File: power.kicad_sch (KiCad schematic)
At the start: 27 parts, among them IC1 SI2301CDS-T1-GE3, J1 Barrel_Jack_MountingPin, J2 Conn_02x04_Odd_Even, U1 TMA-1212D, U2 TPS54302

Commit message: TVS fix
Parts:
- added D13, D14: SMBJ15CA, Diode_SMD:D_SMB, symbol Device:D_TVS
- D1: value D_TVS -> SMBJ15CA
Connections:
- net GND: now also D13.2 (A2), D14.2 (A2)
- net at C2.1, L2.1, U1.6 (+Vout): now also D13.1 (A1), D14.1 (A1)
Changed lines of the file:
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@@
 	)
 	(junction
+		(at 87.63 147.32)
+		(diameter 0)
+		(color 0 0 0 0)
+	)
+	(junction
 		(at 80.01 133.35)
 		(diameter 0)
@@
 	)
 	(junction
+		(at 82.55 128.27)
+		(diameter 0)
+		(color 0 0 0 0)
+	)
+	(junction
 		(at 91.44 49.53)
 		(diameter 0)
@@
 	)
 	(junction
+		(at 93.98 128.27)
+		(diameter 0)
+		(color 0 0 0 0)
+	)
+	(junction
 		(at 161.29 88.9)
 		(diameter 0)
@@
 	(wire
 		(pts
+			(xy 80.01 147.32) (xy 80.01 165.1)
+		)
+		(stroke
+			(width 0)
+			(type default)
+		)
+	)
+	(wire
+		(pts
 			(xy 231.14 128.27) (xy 233.68 128.27)
 		)
@@
 	(wire
 		(pts
-			(xy 71.12 128.27) (xy 88.9 128.27)
+			(xy 71.12 128.27) (xy 82.55 128.27)
 		)
 		(stroke
@@
 	(wire
 		(pts
+			(xy 87.63 152.4) (xy 87.63 147.32)
+		)
+		(stroke
+			(width 0)
+			(type default)
+		)
+	)
+	(wire
+		(pts
 			(xy 80.01 133.35) (xy 95.25 133.35)
 		)
@@
 	(wire
 		(pts
+			(xy 93.98 152.4) (xy 87.63 152.4)
+		)
+		(stroke
+			(width 0)
+			(type default)
+		)
+	)
+	(wire
+		(pts
 			(xy 156.21 118.11) (xy 132.08 118.11)
 		)
@@
 	(wire
 		(pts
-			(xy 80.01 144.78) (xy 80.01 147.32)
-		)
-		(stroke
-			(width 0)
-			(type default)
-		)
-	)
-	(wire
-		(pts
 			(xy 50.8 133.35) (xy 49.53 133.35)
 		)
@@
 	(wire
 		(pts
-			(xy 88.9 147.32) (xy 80.01 147.32)
+			(xy 88.9 147.32) (xy 87.63 147.32)
 		)
 		(stroke
@@
 	(wire
 		(pts
+			(xy 82.55 128.27) (xy 88.9 128.27)
+		)
+		(stroke
+			(width 0)
+			(type default)
+		)
+	)
+	(wire
+		(pts
 			(xy 71.12 133.35) (xy 80.01 133.35)
 		)
@@
 	(wire
 		(pts
+			(xy 82.55 128.27) (xy 82.55 157.48)
+		)
+		(stroke
+			(width 0)
+			(type default)
+		)
+	)
+	(wire
+		(pts
 			(xy 140.97 66.04) (xy 140.97 62.23)
 		)
@@
 	(wire
 		(pts
+			(xy 82.55 165.1) (xy 80.01 165.1)
+		)
+		(stroke
+			(width 0)
+			(type default)
+		)
+	)
+	(wire
+		(pts
 			(xy 205.74 134.62) (xy 214.63 134.62)
 		)
@@
 	(wire
 		(pts
+			(xy 93.98 128.27) (xy 100.33 128.27)
+		)
+		(stroke
+			(width 0)
+			(type default)
+		)
+	)
+	(wire
+		(pts
 			(xy 80.01 49.53) (xy 74.93 49.53)
 		)
@@
 	(wire
 		(pts
-			(xy 88.9 128.27) (xy 100.33 128.27)
+			(xy 88.9 128.27) (xy 93.98 128.27)
 		)
 		(stroke
@@
 	(wire
 		(pts
+			(xy 93.98 144.78) (xy 93.98 128.27)
+		)
+		(stroke
+			(width 0)
+			(type default)
+		)
+	)
+	(wire
+		(pts
+			(xy 87.63 147.32) (xy 80.01 147.32)
+		)
+		(stroke
+			(width 0)
+			(type default)
+		)
+	)
+	(wire
+		(pts
 			(xy 184.15 129.54) (xy 184.15 133.35)
 		)
@@
 		)
 	)
+	(wire
+		(pts
+			(xy 80.01 144.78) (xy 80.01 147.32)
+		)
+		(stroke
+			(width 0)
+			(type default)
+		)
+	)
 	(label "+12V_IN"
 		(at 39.37 46.99 0)
@@
 	)
 	(symbol
+		(lib_id "Device:D_TVS")
+		(at 82.55 161.29 270)
+		(unit 1)
+		(exclude_from_sim no)
+		(in_bom yes)
+		(on_board yes)
+		(dnp no)
+		(property "Reference" "D14"
+			(at 84.836 155.956 90)
+			(effects
+				(font
+					(size 1.27 1.27)
+				)
+			)
+		)
+		(property "Value" "SMBJ15CA"
+			(at 87.63 157.734 90)
+			(effects
+				(font
+					(size 1.27 1.27)
+				)
+			)
+		)
+		(property "Footprint" "Diode_SMD:D_SMB"
+			(at 82.55 161.29 0)
+			(effects
+				(font
+					(size 1.27 1.27)
+				)
+				(hide yes)
+			)
+		)
+		(property "Datasheet" "~"
+			(at 82.55 161.29 0)
+			(effects
+				(font
+					(size 1.27 1.27)
+				)
+				(hide yes)
+			)
+		)
+		(property "Description" "Bidirectional transient-voltage-suppression diode"
+			(at 82.55 161.29 0)
+			(effects
+				(font
+					(size 1.27 1.27)
+				)
+				(hide yes)
+			)
+		)
+		(pin "1"
+		)
+		(pin "2"
+		)
+		(instances
+			(project "daisy-studio"
+				(path "/55cca6a8-30da-4c13-b2f2-a01401e2b54c/a1b2c3d4-1111-4000-8000-000000000001"
+					(reference "D14")
+					(unit 1)
+				)
+			)
+		)
+	)
+	(symbol
 		(lib_id "Device:L")
 		(at 99.06 133.35 90)
@@
 			)
 		)
-		(property "Value" "D_TVS"
+		(property "Value" "SMBJ15CA"
 			(at 85.09 53.594 90)
 			(effects
@@
 					(size 1.27 1.27)
 				)
+				(hide yes)
 			)
 		)
@@
 					(size 1.27 1.27)
 				)
+				(hide yes)
 			)
 		)
@@
 					(unit 1)
 				)
+			)
+		)
+	)
+	(symbol
+		(lib_id "Device:D_TVS")
+		(at 93.98 148.59 270)
+		(unit 1)
+		(exclude_from_sim no)
+		(in_bom yes)
+		(on_board yes)
+		(dnp no)
+		(property "Reference" "D13"
+			(at 96.266 143.256 90)
+			(effects
+				(font
+					(size 1.27 1.27)
+				)
+			)
+		)
+		(property "Value" "SMBJ15CA"
+			(at 99.06 145.034 90)
+			(effects
+				(font
+					(size 1.27 1.27)
+				)
+			)
+		)
+		(property "Footprint" "Diode_SMD:D_SMB"
+			(at 93.98 148.59 0)
+			(effects
+				(font
+					(size 1.27 1.27)
+				)
+				(hide yes)
+			)
+		)
+		(property "Datasheet" "~"
+			(at 93.98 148.59 0)
+			(effects
+				(font
+					(size 1.27 1.27)
+				)
+				(hide yes)
+			)
+		)
+		(property "Description" "Bidirectional transient-voltage-suppression diode"
+			(at 93.98 148.59 0)
+			(effects
+				(font
+					(size 1.27 1.27)
+				)
+				(hide yes)
+			)
+		)
+		(pin "1"
+		)
+		(pin "2"
+		)
+		(instances
+			(project "daisy-studio"
+				(path "/55cca6a8-30da-4c13-b2f2-a01401e2b54c/a1b2c3d4-1111-4000-8000-000000000001"
+					(reference "D13")
+					(unit 1)
+				)

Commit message: working on output
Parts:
- removed J2: Conn_02x04_Odd_Even, Connector_PinHeader_2.54mm:PinHeader_2x04_P2.54mm_Vertical, symbol Connector_Generic:Conn_02x04_Odd_Even
- added J14: Conn_02x04_Odd_Even, Connector_PinHeader_2.54mm:PinHeader_2x04_P2.54mm_Vertical, symbol Connector:Conn_01x04_Pin
- added J2: Conn_02x04_Odd_Even, Connector_PinHeader_2.54mm:PinHeader_2x04_P2.54mm_Vertical, symbol Connector:Conn_01x05_Pin
- renumbered D14 to D2, D13 to D3
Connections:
- net +12VA: now also D2.2 (A2), J2.1 (Pin_1)
- net +3V3A: now also J2.3 (Pin_3)
- net +3V3D: now also J14.1 (Pin_1)
- net +5V: now also J14.4 (Pin_4)
- net -12VA: now also D3.1 (A1), J2.5 (Pin_5)
- net GND: now also D2.1 (A1), J14.2 (Pin_2), J14.3 (Pin_3), J2.2 (Pin_2), J2.4 (Pin_4); no longer D2.2 (A2)
- net at C2.1, L2.1, U1.6 (+Vout): no longer D2.1 (A1), D3.1 (A1)
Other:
- moved on the sheet: D2, D3

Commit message: fix seed schematic
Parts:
- renumbered J14 to J3
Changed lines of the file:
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@@
 		(on_board yes)
 		(dnp no)
-		(property "Reference" "#PWR013"
+		(property "Reference" "#PWR014"
 			(at 190.5 132.08 0)
 			(effects
@@
 			(project "daisy-studio"
 				(path "/55cca6a8-30da-4c13-b2f2-a01401e2b54c/a1b2c3d4-1111-4000-8000-000000000001"
-					(reference "#PWR013")
+					(reference "#PWR014")
 					(unit 1)
 				)
@@
 		(on_board yes)
 		(dnp no)
-		(property "Reference" "#PWR012"
+		(property "Reference" "#PWR013"
 			(at 168.91 148.59 0)
 			(effects
@@
 			(project "triptech"
 				(path "/55cca6a8-30da-4c13-b2f2-a01401e2b54c/a1b2c3d4-1111-4000-8000-000000000001"
-					(reference "#PWR012")
+					(reference "#PWR013")
 					(unit 1)
 				)
@@
 		(dnp no)
 		(fields_autoplaced yes)
-		(property "Reference" "#PWR014"
+		(property "Reference" "#PWR015"
 			(at 205.74 148.59 0)
 			(effects
@@
 			(project "daisy-studio"
 				(path "/55cca6a8-30da-4c13-b2f2-a01401e2b54c/a1b2c3d4-1111-4000-8000-000000000001"
-					(reference "#PWR014")
+					(reference "#PWR015")
 					(unit 1)
 				)
@@
 		(on_board yes)
 		(dnp no)
-		(property "Reference" "J14"
+		(property "Reference" "J3"
 			(at 160.274 132.588 90)
 			(effects
@@
 			(project "daisy-studio"
 				(path "/55cca6a8-30da-4c13-b2f2-a01401e2b54c/a1b2c3d4-1111-4000-8000-000000000001"
-					(reference "J14")
+					(reference "J3")
 					(unit 1)
 				)
@@
 		(on_board yes)
 		(dnp no)
-		(property "Reference" "#PWR016"
+		(property "Reference" "#PWR017"
 			(at 231.14 149.86 0)
 			(effects
@@
 			(project "daisy-studio"
 				(path "/55cca6a8-30da-4c13-b2f2-a01401e2b54c/a1b2c3d4-1111-4000-8000-000000000001"
-					(reference "#PWR016")
+					(reference "#PWR017")
 					(unit 1)
 				)
@@
 		(dnp no)
 		(fields_autoplaced yes)
-		(property "Reference" "#PWR015"
+		(property "Reference" "#PWR016"
 			(at 210.82 96.52 0)
 			(effects
@@
 			(project "triptech"
 				(path "/55cca6a8-30da-4c13-b2f2-a01401e2b54c/a1b2c3d4-1111-4000-8000-000000000001"
-					(reference "#PWR015")
+					(reference "#PWR016")
 					(unit 1)
 				)
@@
 		(dnp no)
 		(fields_autoplaced yes)
-		(property "Reference" "#PWR089"
+		(property "Reference" "#PWR011"
 			(at 154.94 157.48 0)
 			(effects
@@
 			(project "daisy-studio"
 				(path "/55cca6a8-30da-4c13-b2f2-a01401e2b54c/a1b2c3d4-1111-4000-8000-000000000001"
-					(reference "#PWR089")
+					(reference "#PWR011")
 					(unit 1)
 				)
@@
 		(dnp no)
 		(fields_autoplaced yes)
-		(property "Reference" "#PWR017"
+		(property "Reference" "#PWR018"
 			(at 233.68 52.07 0)
 			(effects
@@
 			(project ""
 				(path "/55cca6a8-30da-4c13-b2f2-a01401e2b54c/a1b2c3d4-1111-4000-8000-000000000001"
-					(reference "#PWR017")
+					(reference "#PWR018")
 					(unit 1)
 				)
@@
 		(on_board yes)
 		(dnp no)
-		(property "Reference" "#PWR011"
+		(property "Reference" "#PWR012"
 			(at 157.48 146.05 0)
 			(effects
@@
 			(project "daisy-studio"
 				(path "/55cca6a8-30da-4c13-b2f2-a01401e2b54c/a1b2c3d4-1111-4000-8000-000000000001"
-					(reference "#PWR011")
+					(reference "#PWR012")
 					(unit 1)
 				)

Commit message: fix up power values
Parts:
- C1, C2: value C -> 10u
- C3, C5: value C -> 100n
- C4: value C_Polarized -> 100u
- C6, C7: value C -> 22u
- C8: value C -> 75p
- L1, L2: value L -> BLM18PG121SN1
- L3: value L -> 10uH
- R1: value R -> 10k
- R2: value R -> 100k
- R3: value R -> 13.7k 1%
- R4: value R -> 49k9 1%
- R5: value R -> 100k 1%
- R6: value R -> 13k3 1%
- renumbered IC1 to Q?
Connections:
- no-connect marks 1 -> 0
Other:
- moved on the sheet: J1

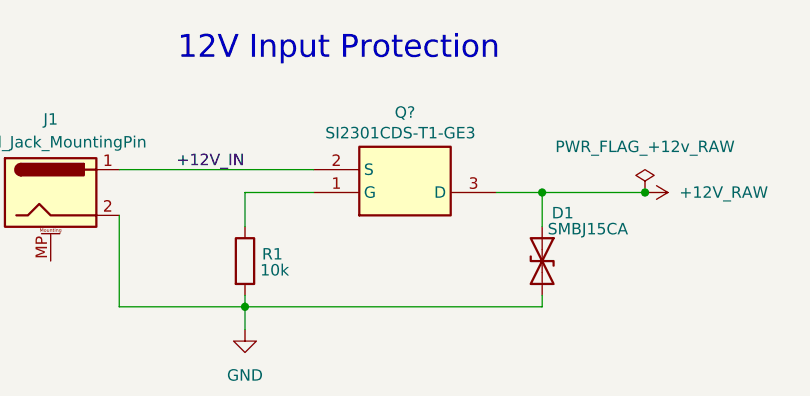
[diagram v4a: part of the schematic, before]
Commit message: reannotate, fix cap footprints
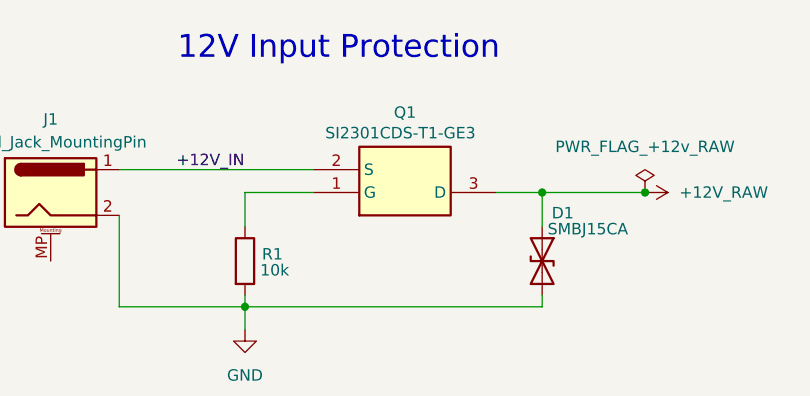
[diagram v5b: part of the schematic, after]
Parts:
- C6, C7: footprint Capacitor_SMD:C_0805_2012Metric -> Capacitor_SMD:C_1206_3216Metric
- gave numbers to parts that had none: 1
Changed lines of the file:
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@@
 			)
 		)
-		(property "Footprint" "Capacitor_SMD:C_0805_2012Metric"
+		(property "Footprint" "Capacitor_SMD:C_1206_3216Metric"
 			(at 211.7852 62.23 0)
 			(effects
@@
 		(on_board yes)
 		(dnp no)
-		(property "Reference" "Q?"
+		(property "Reference" "Q1"
 			(at 64.77 40.64 0)
 			(effects
@@
 			(project "triptech"
 				(path "/55cca6a8-30da-4c13-b2f2-a01401e2b54c/a1b2c3d4-1111-4000-8000-000000000001"
-					(reference "Q?")
+					(reference "Q1")
 					(unit 1)
 				)
@@
 			)
 		)
-		(property "Footprint" "Capacitor_SMD:C_0805_2012Metric"
+		(property "Footprint" "Capacitor_SMD:C_1206_3216Metric"
 			(at 202.8952 62.23 0)
 			(effects

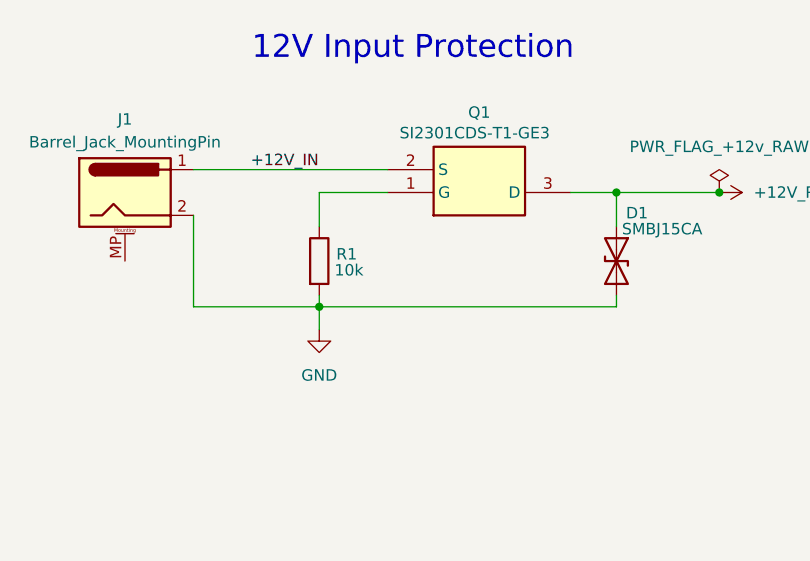
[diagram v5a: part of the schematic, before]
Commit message: add power switch
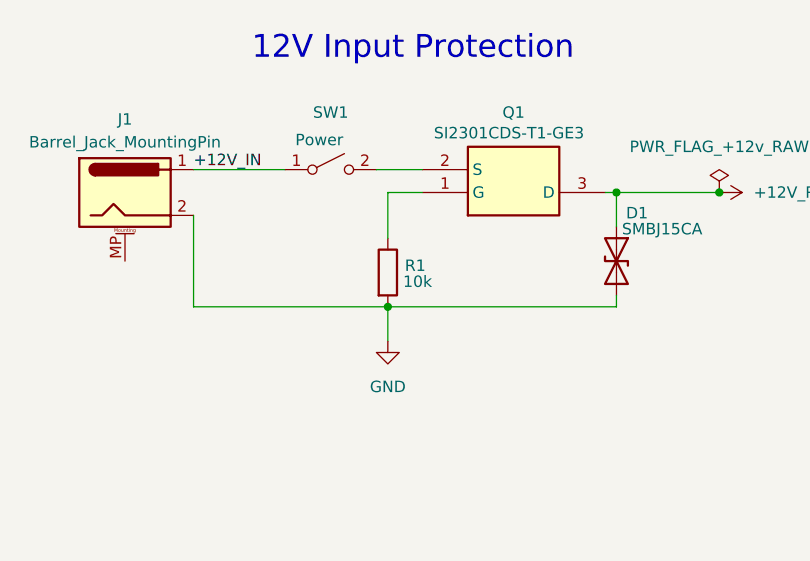
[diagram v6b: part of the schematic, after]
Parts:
- added SW1: Power, Connector_JST:JST_VH_B2P-VH_1x02_P3.96mm_Vertical, symbol Switch:SW_SPST
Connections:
- net +12V_IN: now also SW1.1 (A); no longer Q1.2 (S)
- new net: Q1.2 (S), SW1.2 (B)
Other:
- moved on the sheet: Q1, R1
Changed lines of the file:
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@@
 	)
 	(junction
+		(at 54.61 62.23)
+		(diameter 0)
+		(color 0 0 0 0)
+	)
+	(junction
 		(at 224.79 66.04)
 		(diameter 0)
@@
 	)
 	(junction
-		(at 46.99 62.23)
-		(diameter 0)
-		(color 0 0 0 0)
-	)
-	(junction
 		(at 140.97 62.23)
 		(diameter 0)
@@
 	(wire
 		(pts
-			(xy 46.99 62.23) (xy 46.99 60.96)
-		)
-		(stroke
-			(width 0)
-			(type default)
-		)
-	)
-	(wire
-		(pts
 			(xy 140.97 49.53) (xy 151.13 49.53)
 		)
@@
 	(wire
 		(pts
-			(xy 46.99 64.77) (xy 46.99 62.23)
+			(xy 54.61 66.04) (xy 54.61 62.23)
 		)
 		(stroke
@@
 	(wire
 		(pts
+			(xy 33.02 46.99) (xy 43.18 46.99)
+		)
+		(stroke
+			(width 0)
+			(type default)
+		)
+	)
+	(wire
+		(pts
 			(xy 107.95 128.27) (xy 113.03 128.27)
 		)
@@
 	(wire
 		(pts
-			(xy 210.82 88.9) (xy 210.82 62.23)
+			(xy 54.61 62.23) (xy 80.01 62.23)
 		)
 		(stroke
@@
 	(wire
 		(pts
-			(xy 46.99 49.53) (xy 46.99 53.34)
+			(xy 210.82 88.9) (xy 210.82 62.23)
 		)
 		(stroke
@@
 	(wire
 		(pts
-			(xy 114.3 128.27) (xy 114.3 137.16)
+			(xy 54.61 49.53) (xy 54.61 54.61)
 		)
 		(stroke
@@
 	(wire
 		(pts
-			(xy 113.03 128.27) (xy 114.3 128.27)
+			(xy 114.3 128.27) (xy 114.3 137.16)
 		)
 		(stroke
@@
 	(wire
 		(pts
-			(xy 80.01 133.35) (xy 95.25 133.35)
+			(xy 113.03 128.27) (xy 114.3 128.27)
 		)
 		(stroke
@@
 	(wire
 		(pts
-			(xy 73.66 130.81) (xy 73.66 147.32)
+			(xy 80.01 133.35) (xy 95.25 133.35)
 		)
 		(stroke
@@
 	(wire
 		(pts
-			(xy 124.46 129.54) (xy 124.46 144.78)
+			(xy 73.66 130.81) (xy 73.66 147.32)
 		)
 		(stroke
@@
 	(wire
 		(pts
-			(xy 33.02 46.99) (xy 54.61 46.99)
+			(xy 124.46 129.54) (xy 124.46 144.78)
 		)
 		(stroke
@@
 	(wire
 		(pts
-			(xy 33.02 62.23) (xy 46.99 62.23)
+			(xy 33.02 62.23) (xy 54.61 62.23)
 		)
 		(stroke
@@
 	(wire
 		(pts
-			(xy 80.01 49.53) (xy 74.93 49.53)
+			(xy 80.01 49.53) (xy 78.74 49.53)
 		)
 		(stroke
@@
 	(wire
 		(pts
+			(xy 53.34 46.99) (xy 58.42 46.99)
+		)
+		(stroke
+			(width 0)
+			(type default)
+		)
+	)
+	(wire
+		(pts
 			(xy 148.59 62.23) (xy 140.97 62.23)
 		)
@@
 	(wire
 		(pts
-			(xy 46.99 49.53) (xy 54.61 49.53)
+			(xy 54.61 49.53) (xy 58.42 49.53)
 		)
 		(stroke
@@
 	(wire
 		(pts
-			(xy 46.99 62.23) (xy 80.01 62.23)
-		)
-		(stroke
-			(width 0)
-			(type default)
-		)
-	)
-	(wire
-		(pts
 			(xy 124.46 144.78) (xy 130.81 144.78)
 		)
@@
 	)
 	(label "+12V_IN"
-		(at 39.37 46.99 0)
+		(at 33.02 46.99 0)
 		(effects
 			(font
@@
 	(symbol
 		(lib_id "power:GND")
-		(at 46.99 64.77 0)
+		(at 54.61 66.04 0)
 		(unit 1)
 		(exclude_from_sim no)
@@
 		(fields_autoplaced yes)
 		(property "Reference" "#PWR01"
-			(at 46.99 71.12 0)
+			(at 54.61 72.39 0)
 			(effects
 				(font
@@
 		)
 		(property "Value" "GND"
-			(at 46.99 69.85 0)
+			(at 54.61 71.12 0)
 			(effects
 				(font
@@
 		)
 		(property "Footprint" ""
-			(at 46.99 64.77 0)
+			(at 54.61 66.04 0)
 			(effects
 				(font
@@
 		)
 		(property "Datasheet" ""
-			(at 46.99 64.77 0)
+			(at 54.61 66.04 0)
 			(effects
 				(font
@@
 		)
 		(property "Description" "Power symbol creates a global label with name \"GND\" , ground"
-			(at 46.99 64.77 0)
+			(at 54.61 66.04 0)
 			(effects
 				(font
@@
 	)
 	(symbol
+		(lib_id "Switch:SW_SPST")
+		(at 48.26 46.99 0)
+		(unit 1)
+		(exclude_from_sim no)
+		(in_bom yes)
+		(on_board yes)
+		(dnp no)
+		(property "Reference" "SW1"
+			(at 48.26 40.64 0)
+			(effects
+				(font
+					(size 1.27 1.27)
+				)
+			)
+		)
+		(property "Value" "Power"
+			(at 46.99 43.688 0)
+			(effects
+				(font
+					(size 1.27 1.27)
+				)
+			)
+		)
+		(property "Footprint" "Connector_JST:JST_VH_B2P-VH_1x02_P3.96mm_Vertical"
+			(at 48.26 46.99 0)
+			(effects
+				(font
+					(size 1.27 1.27)
+				)
+				(hide yes)
+			)
+		)
+		(property "Datasheet" "~"
+			(at 48.26 46.99 0)
+			(effects
+				(font
+					(size 1.27 1.27)
+				)
+				(hide yes)
+			)
+		)
+		(property "Description" "Single Pole Single Throw (SPST) switch"
+			(at 48.26 46.99 0)
+			(effects
+				(font
+					(size 1.27 1.27)
+				)
+				(hide yes)
+			)
+		)
+		(pin "1"
+		)
+		(pin "2"
+		)
+		(instances
+			(project ""
+				(path "/55cca6a8-30da-4c13-b2f2-a01401e2b54c/a1b2c3d4-1111-4000-8000-000000000001"
+					(reference "SW1")
+					(unit 1)
+				)
+			)
+		)
+	)
+	(symbol
 		(lib_id "power:+3V3D")
 		(at 149.86 148.59 180)
@@
 	(symbol
 		(lib_id "daisy-studio:SI2301CDS-T1-GE3")
-		(at 54.61 49.53 0)
+		(at 58.42 49.53 0)
 		(mirror x)
 		(unit 1)
@@
 		(dnp no)
 		(property "Reference" "Q1"
-			(at 64.77 40.64 0)
+			(at 68.58 40.64 0)
 			(effects
 				(font
@@
 		)
 		(property "Value" "SI2301CDS-T1-GE3"
-			(at 64.262 42.926 0)
+			(at 68.072 42.926 0)
 			(effects
 				(font
@@
 		)
 		(property "Footprint" "daisy-studio:SOT95P237X112-3N"
-			(at 71.12 -45.39 0)
+			(at 74.93 -45.39 0)
 			(effects
 				(font
@@
 		)
 		(property "Datasheet" "https://www.vishay.com/docs/68741/si2301cd.pdf"
-			(at 71.12 -145.39 0)
+			(at 74.93 -145.39 0)
 			(effects
 				(font
@@
 		)
 		(property "Description" "SI2301CDS-T1-GE3, P-channel MOSFET Transistor 2.3 A 20 V, 3-Pin SOT-23, TO-236"
-			(at 54.61 49.53 0)
+			(at 58.42 49.53 0)
 			(effects
 				(font
@@
 		)
 		(property "Height" "1.12"
-			(at 71.12 -345.39 0)
+			(at 74.93 -345.39 0)
 			(effects
 				(font
@@
 		)
 		(property "Mouser Part Number" "781-SI2301CDS-T1-GE3"
-			(at 71.12 -445.39 0)
+			(at 74.93 -445.39 0)
 			(effects
 				(font
@@
 		)
 		(property "Mouser Price/Stock" "https://www.mouser.co.uk/ProductDetail/Vishay-Semiconductors/SI2301CDS-T1-GE3?qs=IRuQNBqMOcnWEzfGi6KYYw%3D%3D"
-			(at 71.12 -545.39 0)
+			(at 74.93 -545.39 0)
 			(effects
 				(font
@@
 		)
 		(property "Manufacturer_Name" "Vishay"
-			(at 71.12 -645.39 0)
+			(at 74.93 -645.39 0)
 			(effects
 				(font
@@
 		)
 		(property "Manufacturer_Part_Number" "SI2301CDS-T1-GE3"
-			(at 71.12 -745.39 0)
+			(at 74.93 -745.39 0)
 			(effects
 				(font
@@
 	(symbol
 		(lib_id "Device:R")
-		(at 46.99 57.15 0)
+		(at 54.61 58.42 0)
 		(unit 1)
 		(exclude_from_sim no)
@@
 		(dnp no)
 		(property "Reference" "R1"
-			(at 50.038 56.388 0)
+			(at 57.658 57.658 0)
 			(effects
 				(font
@@
 		)
 		(property "Value" "10k"
-			(at 50.292 58.166 0)
+			(at 57.912 59.436 0)
 			(effects
 				(font
@@
 		)
 		(property "Footprint" "Resistor_SMD:R_0805_2012Metric"
-			(at 45.212 57.15 90)
+			(at 52.832 58.42 90)
 			(effects
 				(font
@@
 		)
 		(property "Datasheet" "~"
-			(at 46.99 57.15 0)
+			(at 54.61 58.42 0)
 			(effects
 				(font
@@
 		)
 		(property "Description" "Resistor"
-			(at 46.99 57.15 0)
+			(at 54.61 58.42 0)
 			(effects
 				(font
